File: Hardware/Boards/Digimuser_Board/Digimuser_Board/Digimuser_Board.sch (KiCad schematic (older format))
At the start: 64 parts, among them J1 Conn_01x01, J10 Conn_01x01, J11 Conn_01x01, J12 Conn_01x01, J2 Conn_01x01, J3 Barrel_Jack_MountingPin, J4 Conn_01x03, J5 Conn_01x03, J6 Conn_01x01, J7 Conn_01x01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

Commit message: Last save before making circuit revisions.
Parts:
- added TP?: TestPoint, symbol Connector:TestPoint
- R15: value 1K -> 5K
- R17: value 5K -> 1K
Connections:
- net FILT_OUT: now also TP?.1
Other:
- note added: "GET RID OF THIS"
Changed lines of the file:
@@
 	0    -1   -1   0
 $EndComp
-Text Label 4900 1725 0    50   ~ 0
+Text Label 4825 1725 0    50   ~ 0
 FILT_OUT
 Text Label 3550 1725 0    50   ~ 0
@@
 MIC_IN-\n
 $Comp
-L teensy:Teensy4.0 U4
-U 1 1 5FBC5029
-P 3775 6175
-F 0 "U4" H 3775 7790 50  0000 C CNN
-F 1 "Teensy4.0" H 3775 7699 50  0000 C CNN
-F 2 "teensy:Teensy40_HAT" H 3375 6375 50  0001 C CNN
-F 3 "" H 3375 6375 50  0001 C CNN
-	1    3775 6175
-	1    0    0    -1
-$EndComp
-$Comp
 L CS5343CZZ:CS5343-CZZ U6
 U 1 1 5FBE3551
@@
 P 8250 5600
 F 0 "R17" V 8350 5600 50  0000 C CNN
-F 1 "5K" V 8425 5600 50  0000 C CNN
+F 1 "1K" V 8425 5600 50  0000 C CNN
 F 2 "Resistor_SMD:R_0805_2012Metric" V 8290 5590 50  0001 C CNN
 F 3 "~" H 8250 5600 50  0001 C CNN
@@
 P 7625 5825
 F 0 "R15" H 7500 5850 50  0000 C CNN
-F 1 "1K" H 7475 5925 50  0000 C CNN
+F 1 "5K" H 7475 5925 50  0000 C CNN
 F 2 "Resistor_SMD:R_0805_2012Metric" V 7665 5815 50  0001 C CNN
 F 3 "~" H 7625 5825 50  0001 C CNN
@@
 	7625 5150 7725 5150
 Connection ~ 7625 5600
-Wire Wire Line
-	7625 5975 7625 6100
-$Comp
-L power:GND #PWR016
-U 1 1 5FB97979
-P 7625 6100
-F 0 "#PWR016" H 7625 5850 50  0001 C CNN
-F 1 "GND" H 7630 5927 50  0000 C CNN
-F 2 "" H 7625 6100 50  0001 C CNN
-F 3 "" H 7625 6100 50  0001 C CNN
-	1    7625 6100
-	1    0    0    -1
-$EndComp
 Text GLabel 7400 4950 0    50   Input ~ 0
 DAC_OUT
@@
 	1    0    0    -1
 $EndComp
+$Comp
+L Connector:TestPoint TP?
+U 1 1 5FC657BE
+P 5175 1725
+F 0 "TP?" H 5225 2075 50  0000 L CNN
+F 1 "TestPoint" H 5225 2000 50  0000 L CNN
+F 2 "" H 5375 1725 50  0001 C CNN
+F 3 "~" H 5375 1725 50  0001 C CNN
+	1    5175 1725
+	1    0    0    -1
+$EndComp
+Wire Wire Line
+	7625 5975 7625 6100
+$Comp
+L power:GND #PWR016
+U 1 1 5FB97979
+P 7625 6100
+F 0 "#PWR016" H 7625 5850 50  0001 C CNN
+F 1 "GND" H 7630 5927 50  0000 C CNN
+F 2 "" H 7625 6100 50  0001 C CNN
+F 3 "" H 7625 6100 50  0001 C CNN
+	1    7625 6100
+	1    0    0    -1
+$EndComp
+$Comp
+L teensy:Teensy4.0 U4
+U 1 1 5FBC5029
+P 3775 6175
+F 0 "U4" H 3775 7790 50  0000 C CNN
+F 1 "Teensy4.0" H 3775 7699 50  0000 C CNN
+F 2 "teensy:Teensy40_HAT" H 3375 6375 50  0001 C CNN
+F 3 "" H 3375 6375 50  0001 C CNN
+	1    3775 6175
+	1    0    0    -1
+$EndComp
+Text Notes 6725 4225 0    69   ~ 0
+GET RID OF THIS
 $EndSCHEMATC

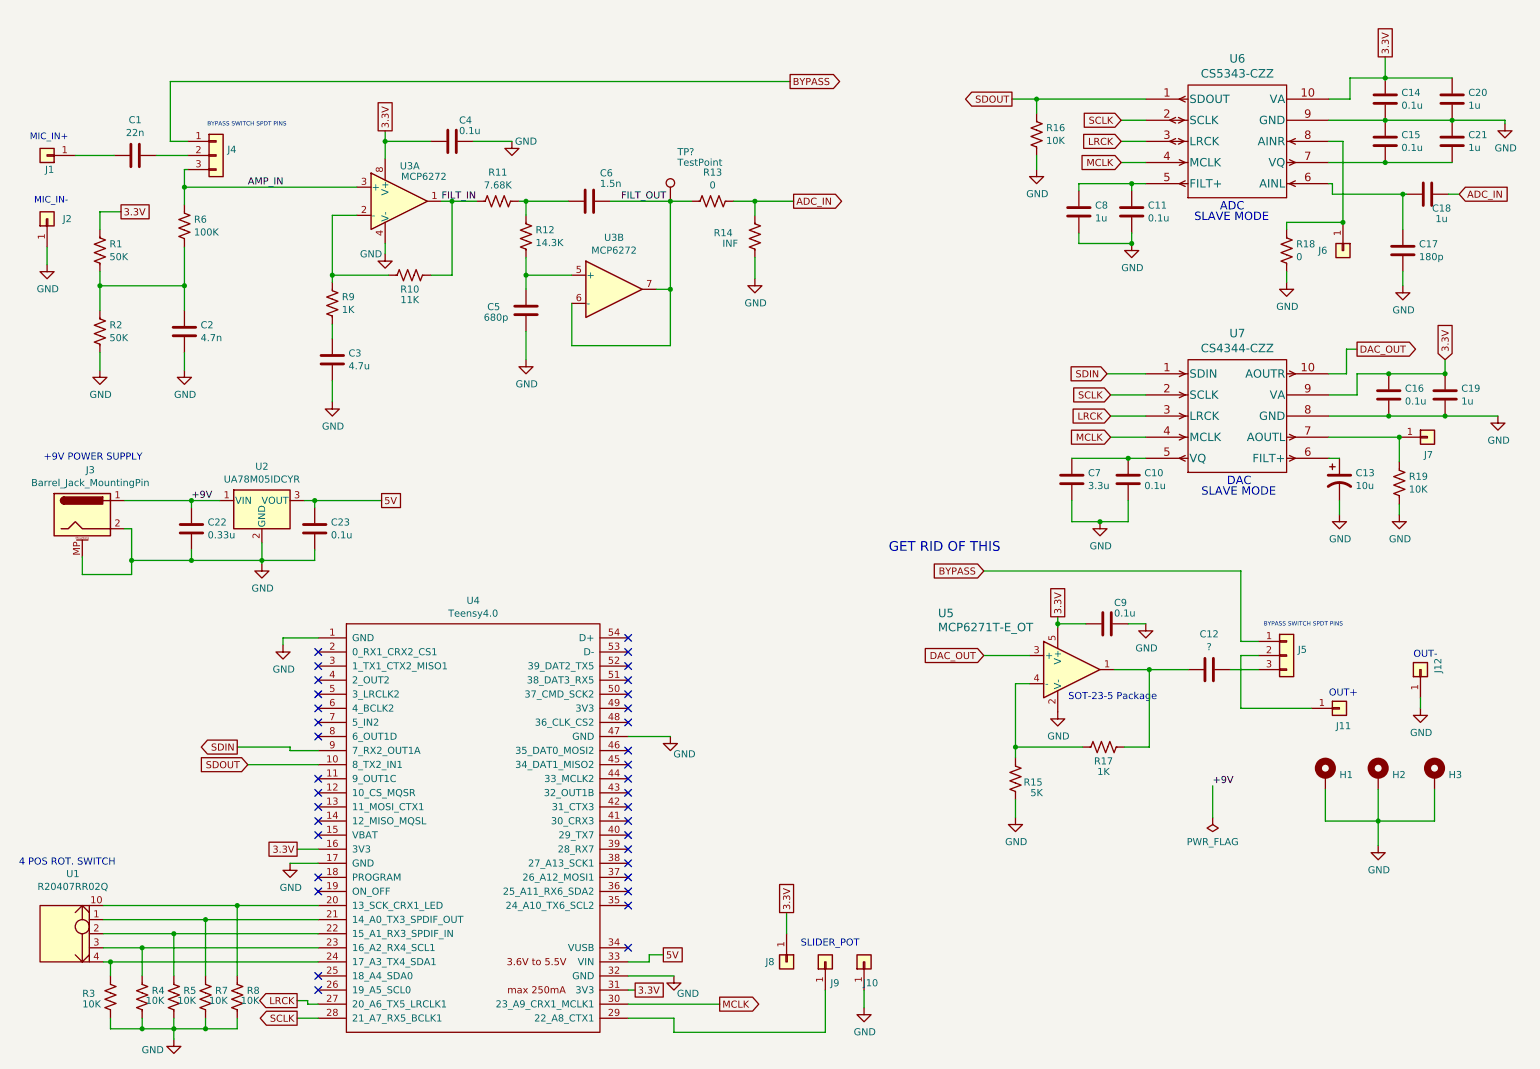
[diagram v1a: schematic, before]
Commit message: Did a re-layout of the PCB and redid the schematic.Ready for review.
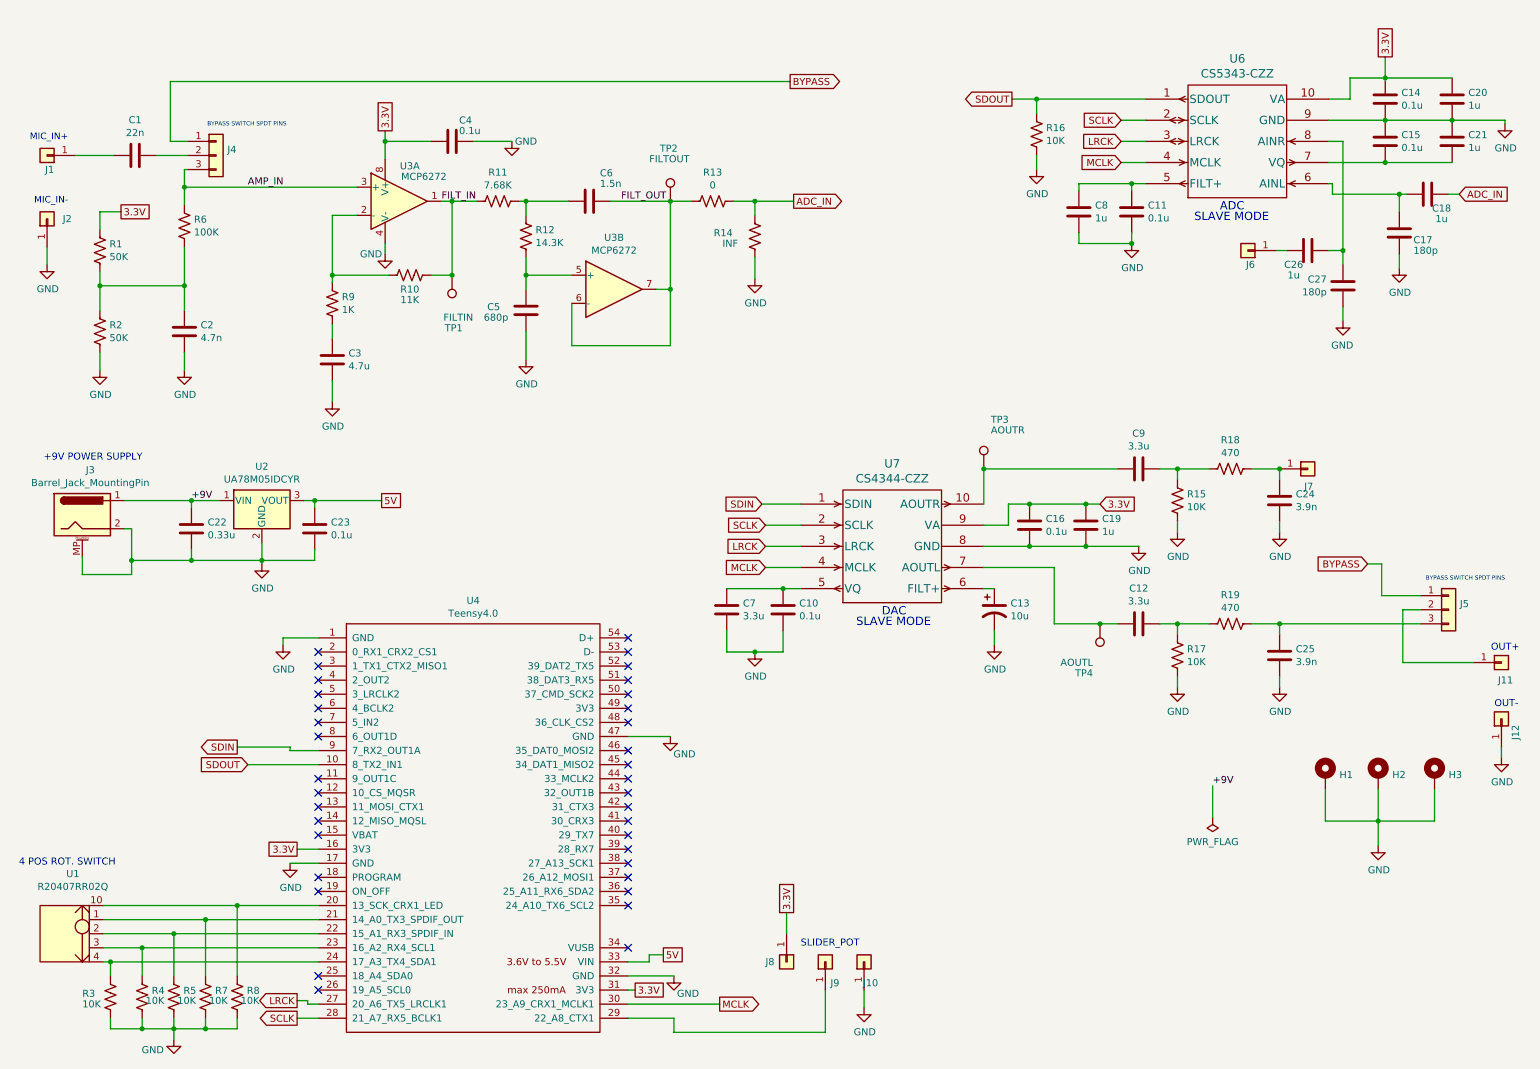
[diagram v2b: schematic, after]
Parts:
- removed U5: MCP6271T-E_OT, MCP6271TE0T:MCP6271T-E&slash_OT, symbol MCP6271TEOT:MCP6271T-E_OT
- added C24, C25: 3.9n, Capacitor_SMD:C_0805_2012Metric, symbol Device:C
- added C26: 1u, Capacitor_SMD:C_0805_2012Metric, symbol Device:C
- added C27: 180p, Capacitor_SMD:C_0805_2012Metric, symbol Device:C
- added TP1: FILTIN, TestPoint:TestPoint_Keystone_5019_Minature, symbol Connector:TestPoint
- added TP3: AOUTR, TestPoint:TestPoint_Keystone_5019_Minature, symbol Connector:TestPoint
- added TP4: AOUTL, TestPoint:TestPoint_Keystone_5019_Minature, symbol Connector:TestPoint
- C12: value ? -> 3.3u
- C9: value 0.1u -> 3.3u
- R15: value 5K -> 10K
- R17: value 1K -> 10K
- R18: value 0 -> 470
- R19: value 10K -> 470
- TP2: renamed from TP?; value TestPoint -> FILTOUT; footprint (none) -> TestPoint:TestPoint_Keystone_5019_Minature
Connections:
- net 3.3V: no longer C9.2
- net FILT_IN: now also TP1.1
- net GND: now also R15.2, R17.2, C24.2, C25.2, C27.2; no longer C9.1, R15.1, R18.2, R19.2
- net at C12.2: now also U7.7 (AOUTL), TP4.1; no longer R17.1
- net at J5.3 (Pin_3): now also R19.1, C25.1; no longer C12.1
- net DAC_OUT: no longer names the net of U7.10 (AOUTR)
- net DAC_OUT: now also C9.2, TP3.1
- new net: C24.1, J7.1 (Pin_1), R18.1
- new net: C26.2, C27.1, U6.8 (AINR)
- new net: C26.1, J6.1 (Pin_1)
- new net: C9.1, R15.1, R18.2
- new net: C12.1, R17.1, R19.2
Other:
- note removed: "GET RID OF THIS"
- note removed: "SOT-23-5 Package"
- moved on the sheet: C10, C13, C16, C17, C19, C7, J11, J12, J5, J6, J7, U7

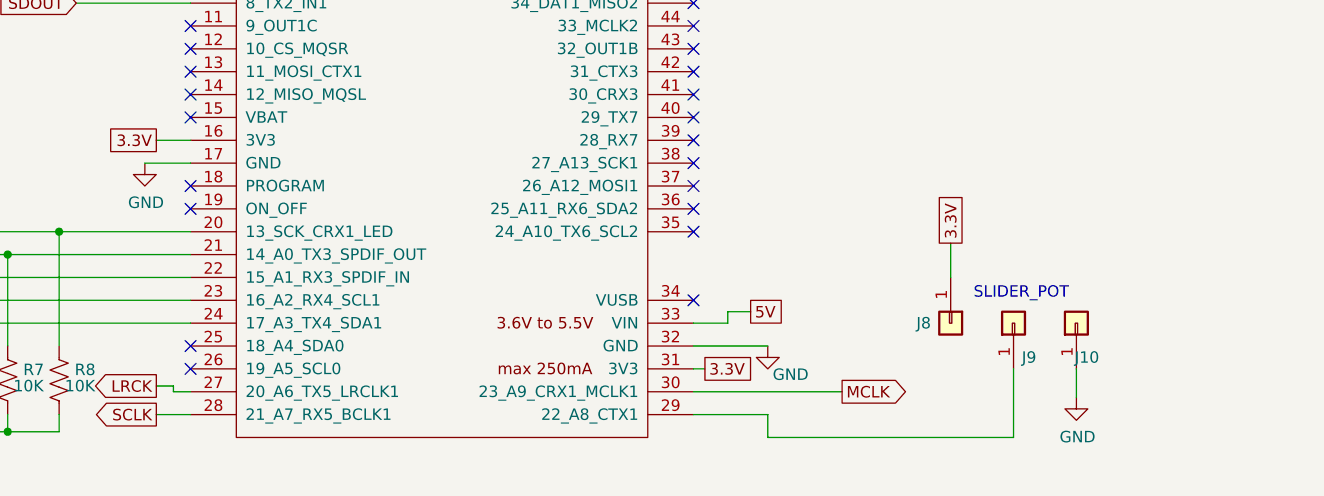
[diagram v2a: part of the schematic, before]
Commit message: Added pin connection for a second potentiometer.
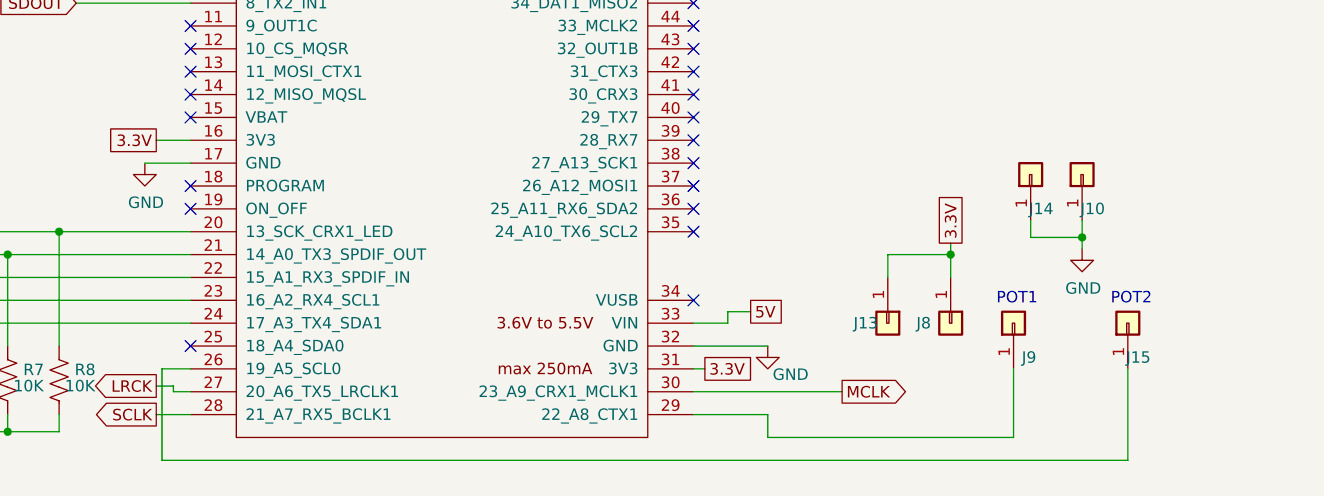
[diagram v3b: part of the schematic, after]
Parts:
- added J13, J14, J15: Conn_01x01, Custom_Connectors:PinHeader_2.54mm_1x01_P2.54mm, symbol Connector_Generic:Conn_01x01
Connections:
- net 3.3V: now also J13.1 (Pin_1)
- net GND: now also J14.1 (Pin_1)
- net at U4.26 (19_A5_SCL0): now also J15.1 (Pin_1)
- no-connect marks 36 -> 35
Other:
- note added: "POT1"
- note added: "POT2"
- note removed: "SLIDER_POT"
- moved on the sheet: J10
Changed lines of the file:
@@
 NoConn ~ 2675 6625
 NoConn ~ 2675 7225
-NoConn ~ 2675 7325
 NoConn ~ 4875 4825
 NoConn ~ 4875 4925
@@
 	4875 7525 5200 7525
 Wire Wire Line
-	6000 6925 6000 6775
+	6000 6925 6000 6825
 Text GLabel 6000 6775 1    50   UnSpc ~ 0
 3.3V
@@
 L power:GND #PWR015
 U 1 1 5FBEF172
-P 6550 7450
-F 0 "#PWR015" H 6550 7200 50  0001 C CNN
-F 1 "GND" H 6555 7277 50  0000 C CNN
-F 2 "" H 6550 7450 50  0001 C CNN
-F 3 "" H 6550 7450 50  0001 C CNN
-	1    6550 7450
+P 6575 6800
+F 0 "#PWR015" H 6575 6550 50  0001 C CNN
+F 1 "GND" H 6580 6627 50  0000 C CNN
+F 2 "" H 6575 6800 50  0001 C CNN
+F 3 "" H 6575 6800 50  0001 C CNN
+	1    6575 6800
 	1    0    0    -1
 $EndComp
@@
 L Connector_Generic:Conn_01x01 J10
 U 1 1 5FC5BD03
-P 6550 7125
-F 0 "J10" V 6400 7025 50  0000 L CNN
-F 1 "Conn_01x01" V 6675 6700 50  0001 L CNN
-F 2 "Custom_Connectors:PinHeader_2.54mm_1x01_P2.54mm" H 6550 7125 50  0001 C CNN
-F 3 "~" H 6550 7125 50  0001 C CNN
-	1    6550 7125
+P 6575 6475
+F 0 "J10" V 6425 6375 50  0000 L CNN
+F 1 "Conn_01x01" V 6700 6050 50  0001 L CNN
+F 2 "Custom_Connectors:PinHeader_2.54mm_1x01_P2.54mm" H 6575 6475 50  0001 C CNN
+F 3 "~" H 6575 6475 50  0001 C CNN
+	1    6575 6475
 	0    -1   -1   0
 $EndComp
 Wire Wire Line
-	6550 7450 6550 7325
+	6575 6800 6575 6750
 $Comp
 L Connector_Generic:Conn_01x01 J8
@@
 	0    1    1    0
 $EndComp
-Text Notes 6100 7025 0    50   ~ 0
-SLIDER_POT
+Text Notes 6200 7050 0    50   ~ 0
+POT1
 $Comp
 L Connector:Barrel_Jack_MountingPin J3
@@
 $EndComp
 $Comp
-L teensy:Teensy4.0 U4
-U 1 1 5FBC5029
-P 3775 6175
-F 0 "U4" H 3775 7790 50  0000 C CNN
-F 1 "Teensy4.0" H 3775 7699 50  0000 C CNN
-F 2 "teensy:Teensy40_HAT" H 3375 6375 50  0001 C CNN
-F 3 "" H 3375 6375 50  0001 C CNN
-	1    3775 6175
-	1    0    0    -1
-$EndComp
-$Comp
 L Device:C C9
 U 1 1 5FD2CDAC
@@
 	9500 4725 10500 4725
 Connection ~ 9500 3625
+$Comp
+L Connector_Generic:Conn_01x01 J15
+U 1 1 5FC8AFE7
+P 6775 7125
+F 0 "J15" V 6625 7025 50  0000 L CNN
+F 1 "Conn_01x01" V 6900 6700 50  0001 L CNN
+F 2 "Custom_Connectors:PinHeader_2.54mm_1x01_P2.54mm" H 6775 7125 50  0001 C CNN
+F 3 "~" H 6775 7125 50  0001 C CNN
+	1    6775 7125
+	0    -1   -1   0
+$EndComp
+$Comp
+L teensy:Teensy4.0 U4
+U 1 1 5FBC5029
+P 3775 6175
+F 0 "U4" H 3775 7790 50  0000 C CNN
+F 1 "Teensy4.0" H 3775 7699 50  0000 C CNN
+F 2 "teensy:Teensy40_HAT" H 3375 6375 50  0001 C CNN
+F 3 "" H 3375 6375 50  0001 C CNN
+	1    3775 6175
+	1    0    0    -1
+$EndComp
+Wire Wire Line
+	2550 7325 2550 7725
+Wire Wire Line
+	2550 7725 6775 7725
+Wire Wire Line
+	6775 7725 6775 7325
+Wire Wire Line
+	2550 7325 2675 7325
+Text Notes 6700 7050 0    50   ~ 0
+POT2
+$Comp
+L Connector_Generic:Conn_01x01 J13
+U 1 1 5FC9BEE5
+P 5725 7125
+F 0 "J13" V 5725 6975 50  0000 L CNN
+F 1 "Conn_01x01" V 5850 6700 50  0001 L CNN
+F 2 "Custom_Connectors:PinHeader_2.54mm_1x01_P2.54mm" H 5725 7125 50  0001 C CNN
+F 3 "~" H 5725 7125 50  0001 C CNN
+	1    5725 7125
+	0    1    1    0
+$EndComp
+Wire Wire Line
+	6000 6825 5725 6825
+Wire Wire Line
+	5725 6825 5725 6925
+Connection ~ 6000 6825
+Wire Wire Line
+	6000 6825 6000 6775
+$Comp
+L Connector_Generic:Conn_01x01 J14
+U 1 1 5FCB954D
+P 6350 6475
+F 0 "J14" V 6200 6375 50  0000 L CNN
+F 1 "Conn_01x01" V 6475 6050 50  0001 L CNN
+F 2 "Custom_Connectors:PinHeader_2.54mm_1x01_P2.54mm" H 6350 6475 50  0001 C CNN
+F 3 "~" H 6350 6475 50  0001 C CNN
+	1    6350 6475
+	0    -1   -1   0
+$EndComp
+Wire Wire Line
+	6575 6750 6350 6750
+Wire Wire Line
+	6350 6750 6350 6675
+Connection ~ 6575 6750
+Wire Wire Line
+	6575 6750 6575 6675
 $EndSCHEMATC

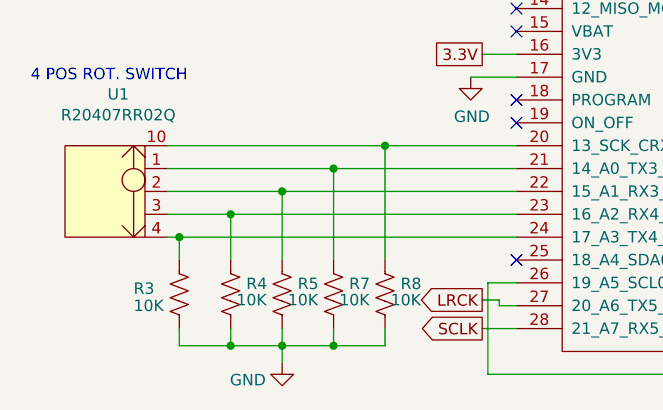
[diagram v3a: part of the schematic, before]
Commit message: Sent board out for review. Received feedback and made changes to the PCB layout accordingly. Changes include: Pin headers spaced 0.1in, Labeling Teensy connection pins, updating voltage regulator GNDing. Board sent for a second review. Currently on RevA1 for DIGIMUSER.
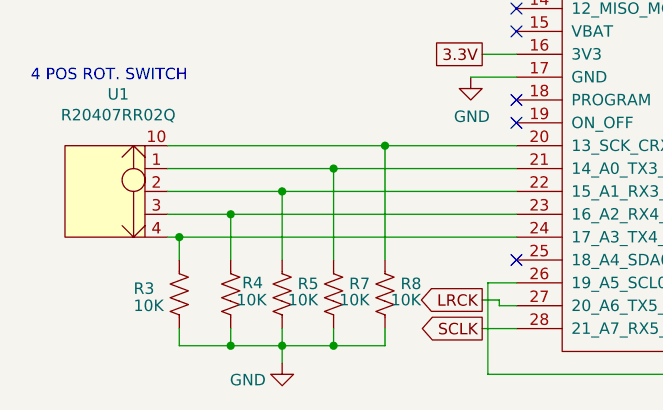
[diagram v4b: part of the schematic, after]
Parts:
- U2: footprint Package_TO_SOT_SMD:SOT-223 -> Package_TO_SOT_SMD:SOT-223-3_TabPin2
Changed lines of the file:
@@
 Title "Digimuser Board"
 Date "2020-11-12"
-Rev "A"
+Rev "A1"
 Comp "Author: David Pierce Walker-Howell"
 Comment1 ""
@@
 U 1 1 5FCB0650
 P 1425 7375
-F 0 "R4" H 1493 7421 50  0000 L CNN
+F 0 "R4" H 1475 7425 50  0000 L CNN
 F 1 "10K" H 1450 7350 50  0000 L CNN
 F 2 "Resistor_SMD:R_0805_2012Metric" V 1465 7365 50  0001 C CNN
@@
 F 0 "U2" H 2275 4092 50  0000 C CNN
 F 1 "UA78M05IDCYR" H 2275 4001 50  0000 C CNN
-F 2 "Package_TO_SOT_SMD:SOT-223" H 2275 4075 50  0001 C CNN
+F 2 "Package_TO_SOT_SMD:SOT-223-3_TabPin2" H 2275 4075 50  0001 C CNN
 F 3 "https://www.diodes.com/assets/Datasheets/AP2204.pdf" H 2275 3850 50  0001 C CNN
 	1    2275 3850

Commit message: Finished final details for first prototype.
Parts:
- C24, C25: value 3.9n -> 3.3n
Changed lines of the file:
@@
 P 9500 3850
 F 0 "C24" H 9615 3896 50  0000 L CNN
-F 1 "3.9n" H 9615 3805 50  0000 L CNN
+F 1 "3.3n" H 9615 3805 50  0000 L CNN
 F 2 "Capacitor_SMD:C_0805_2012Metric" H 9538 3700 50  0001 C CNN
 F 3 "~" H 9500 3850 50  0001 C CNN
@@
 P 9500 4950
 F 0 "C25" H 9615 4996 50  0000 L CNN
-F 1 "3.9n" H 9615 4905 50  0000 L CNN
+F 1 "3.3n" H 9615 4905 50  0000 L CNN
 F 2 "Capacitor_SMD:C_0805_2012Metric" H 9538 4800 50  0001 C CNN
 F 3 "~" H 9500 4950 50  0001 C CNN
